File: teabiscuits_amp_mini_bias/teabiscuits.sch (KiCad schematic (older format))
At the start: 15 parts, among them J1 Conn_Coaxial, J2 Conn_Coaxial, J3 Conn_01x03_Male, J4 Conn_Coaxial, U2 LMP7721, U3 OP07

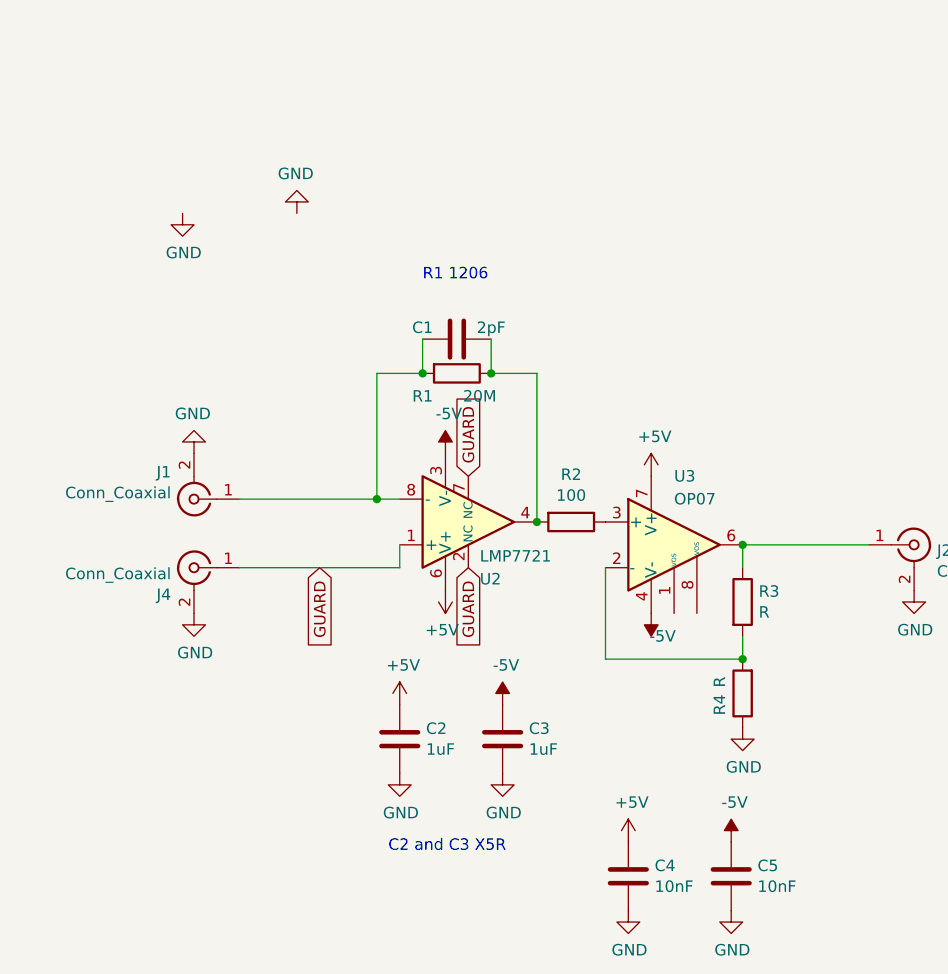
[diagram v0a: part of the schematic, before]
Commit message: Amplifier with bias updated to correct for offset
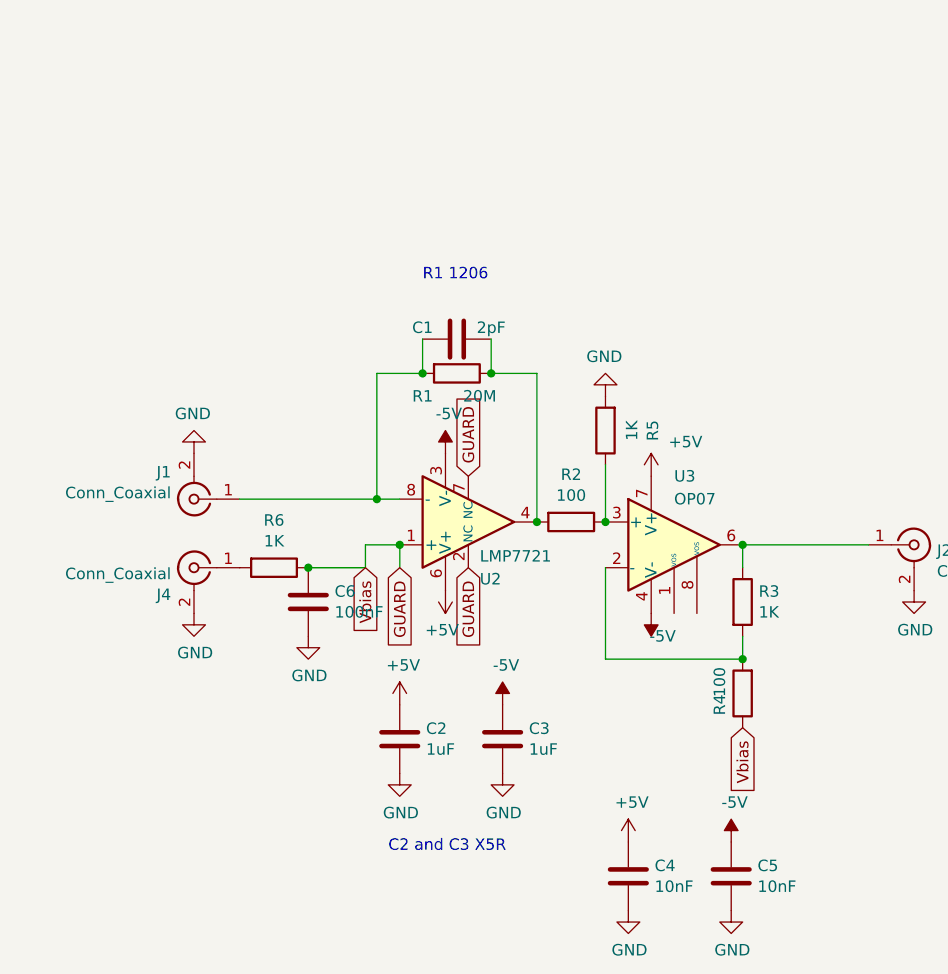
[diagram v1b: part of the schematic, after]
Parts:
- added C6: 100nF, Capacitor_SMD:C_0805_2012Metric, symbol Device:C
- added R5, R6: 1K, Resistor_SMD:R_0805_2012Metric, symbol Device:R
- R3: value R -> 1K
- R4: value R -> 100
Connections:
- net GND: now also C6.2, R5.2; no longer R4.1
- net GUARD: now also R4.1, C6.1, R6.1; no longer J4.1 (In)
- net at R2.1, U3.3 (+): now also R5.1
- new net: J4.1 (In), R6.2
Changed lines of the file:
@@
 P 7750 3450
 F 0 "R3" H 7820 3496 50  0000 L CNN
-F 1 "R" H 7820 3405 50  0000 L CNN
+F 1 "1K" H 7820 3405 50  0000 L CNN
 F 2 "Resistor_SMD:R_0805_2012Metric" V 7680 3450 50  0001 C CNN
 F 3 "~" H 7750 3450 50  0001 C CNN
@@
 P 7750 3850
 F 0 "R4" V 7850 3900 50  0000 C CNN
-F 1 "R" V 7850 3800 50  0000 C CNN
+F 1 "100" V 7850 3800 50  0000 C CNN
 F 2 "Resistor_SMD:R_0805_2012Metric" V 7680 3850 50  0001 C CNN
 F 3 "~" H 7750 3850 50  0001 C CNN
@@
 Wire Wire Line
 	7750 3600 7750 3700
-Wire Wire Line
-	7750 3700 7150 3700
-Wire Wire Line
-	7150 3300 7150 3700
 Connection ~ 7750 3700
 $Comp
@@
 P 7350 2900
 F 0 "#PWR0113" H 7350 2750 50  0001 C CNN
-F 1 "+5V" H 7365 3073 50  0000 C CNN
+F 1 "+5V" H 7500 3050 50  0000 C CNN
 F 2 "" H 7350 2900 50  0001 C CNN
 F 3 "" H 7350 2900 50  0001 C CNN
 	1    7350 2900
-	1    0    0    -1
-$EndComp
-$Comp
-L power:GND #PWR0114
-U 1 1 5EF4FFFA
-P 7750 4000
-F 0 "#PWR0114" H 7750 3750 50  0001 C CNN
-F 1 "GND" H 7755 3827 50  0000 C CNN
-F 2 "" H 7750 4000 50  0001 C CNN
-F 3 "" H 7750 4000 50  0001 C CNN
-	1    7750 4000
 	1    0    0    -1
 $EndComp
@@
 F 3 "" H 8500 3400 50  0001 C CNN
 	1    8500 3400
-	1    0    0    -1
-$EndComp
-$Comp
-L power:GND #PWR0120
-U 1 1 5EF6C887
-P 5800 1750
-F 0 "#PWR0120" H 5800 1500 50  0001 C CNN
-F 1 "GND" H 5805 1577 50  0000 C CNN
-F 2 "" H 5800 1750 50  0001 C CNN
-F 3 "" H 5800 1750 50  0001 C CNN
-	1    5800 1750
-	-1   0    0    1
-$EndComp
-$Comp
-L power:GND #PWR0101
-U 1 1 5EF786C0
-P 5300 1750
-F 0 "#PWR0101" H 5300 1500 50  0001 C CNN
-F 1 "GND" H 5305 1577 50  0000 C CNN
-F 2 "" H 5300 1750 50  0001 C CNN
-F 3 "" H 5300 1750 50  0001 C CNN
-	1    5300 1750
 	1    0    0    -1
 $EndComp
@@
 	-1   0    0    -1
 $EndComp
-Wire Wire Line
-	6250 3300 5550 3300
 $Comp
 L power:GND #PWR0121
@@
 	1    0    0    -1
 $EndComp
-Text GLabel 5900 3300 3    50   Input ~ 0
+Text GLabel 6250 3300 3    50   Input ~ 0
 GUARD
 Text GLabel 6550 3300 3    50   Input ~ 0
@@
 Text GLabel 6550 2900 1    50   Input ~ 0
 GUARD
+Wire Wire Line
+	7750 3700 7150 3700
+Wire Wire Line
+	7150 3700 7150 3300
+Text GLabel 7750 4000 3    50   Input ~ 0
+Vbias
+Text GLabel 6100 3300 3    50   Input ~ 0
+Vbias
+$Comp
+L Device:R R5
+U 1 1 5F28453F
+P 7150 2700
+F 0 "R5" V 6943 2700 50  0000 C CNN
+F 1 "1K" V 7034 2700 50  0000 C CNN
+F 2 "Resistor_SMD:R_0805_2012Metric" V 7080 2700 50  0001 C CNN
+F 3 "~" H 7150 2700 50  0001 C CNN
+	1    7150 2700
+	-1   0    0    1
+$EndComp
+Connection ~ 7150 3100
+$Comp
+L power:GND #PWR01
+U 1 1 5F284AEF
+P 7150 2550
+F 0 "#PWR01" H 7150 2300 50  0001 C CNN
+F 1 "GND" H 7155 2377 50  0000 C CNN
+F 2 "" H 7150 2550 50  0001 C CNN
+F 3 "" H 7150 2550 50  0001 C CNN
+	1    7150 2550
+	-1   0    0    1
+$EndComp
+Wire Wire Line
+	7150 2850 7150 3100
+$Comp
+L Device:R R6
+U 1 1 5F28EE92
+P 5700 3300
+F 0 "R6" V 5493 3300 50  0000 C CNN
+F 1 "1K" V 5584 3300 50  0000 C CNN
+F 2 "Resistor_SMD:R_0805_2012Metric" V 5630 3300 50  0001 C CNN
+F 3 "~" H 5700 3300 50  0001 C CNN
+	1    5700 3300
+	0    1    1    0
+$EndComp
+Wire Wire Line
+	5850 3300 6100 3300
+Wire Wire Line
+	6250 3200 6100 3200
+Wire Wire Line
+	6100 3200 6100 3300
+Connection ~ 6250 3200
+$Comp
+L Device:C C6
+U 1 1 5F28FF65
+P 5850 3450
+F 0 "C6" H 5965 3496 50  0000 L CNN
+F 1 "100nF" H 5965 3405 50  0000 L CNN
+F 2 "Capacitor_SMD:C_0805_2012Metric" H 5888 3300 50  0001 C CNN
+F 3 "~" H 5850 3450 50  0001 C CNN
+	1    5850 3450
+	1    0    0    -1
+$EndComp
+Connection ~ 5850 3300
+$Comp
+L power:GND #PWR02
+U 1 1 5F290867
+P 5850 3600
+F 0 "#PWR02" H 5850 3350 50  0001 C CNN
+F 1 "GND" H 5855 3427 50  0000 C CNN
+F 2 "" H 5850 3600 50  0001 C CNN
+F 3 "" H 5850 3600 50  0001 C CNN
+	1    5850 3600
+	1    0    0    -1
+$EndComp
 $EndSCHEMATC

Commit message: Fixes to compute board
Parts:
- C2, C3: value 1uF -> 100nF
- R1: value 20M -> 1M
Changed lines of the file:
@@
 P 6500 2450
 F 0 "R1" V 6600 2300 50  0000 C CNN
-F 1 "20M" V 6600 2550 50  0000 C CNN
+F 1 "1M" V 6600 2550 50  0000 C CNN
 F 2 "Resistor_SMD:R_1206_3216Metric" V 6430 2450 50  0001 C CNN
 F 3 "~" H 6500 2450 50  0001 C CNN
@@
 P 6250 4050
 F 0 "C2" H 6365 4096 50  0000 L CNN
-F 1 "1uF" H 6365 4005 50  0000 L CNN
+F 1 "100nF" H 6365 4005 50  0000 L CNN
 F 2 "Capacitor_SMD:C_0805_2012Metric" H 6288 3900 50  0001 C CNN
 F 3 "~" H 6250 4050 50  0001 C CNN
@@
 P 6700 4050
 F 0 "C3" H 6815 4096 50  0000 L CNN
-F 1 "1uF" H 6815 4005 50  0000 L CNN
+F 1 "100nF" H 6815 4005 50  0000 L CNN
 F 2 "Capacitor_SMD:C_0805_2012Metric" H 6738 3900 50  0001 C CNN
 F 3 "~" H 6700 4050 50  0001 C CNN

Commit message: Current board designs
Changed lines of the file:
@@
 U 1 1 5EF3B232
 P 7750 3850
-F 0 "R4" V 7850 3900 50  0000 C CNN
+F 0 "R4" H 7850 3950 50  0000 C CNN
 F 1 "100" V 7850 3800 50  0000 C CNN
 F 2 "Resistor_SMD:R_0805_2012Metric" V 7680 3850 50  0001 C CNN
@@
 U 1 1 5F28FF65
 P 5850 3450
-F 0 "C6" H 5965 3496 50  0000 L CNN
-F 1 "100nF" H 5965 3405 50  0000 L CNN
+F 0 "C6" H 5850 3350 50  0000 L CNN
+F 1 "100nF" H 5600 3350 50  0000 L CNN
 F 2 "Capacitor_SMD:C_0805_2012Metric" H 5888 3300 50  0001 C CNN
 F 3 "~" H 5850 3450 50  0001 C CNN
